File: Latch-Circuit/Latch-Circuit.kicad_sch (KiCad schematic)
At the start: 85 parts, among them J1 BM02B-PASS-1-TF, J10 BM02B-PASS-1-TF, J2 BM03B-PASS-1-TF, J3 BM02B-PASS-1-TF, J4 BM02B-PASS-1-TF, J5 BM02B-PASS-1-TF, J6 BM02B-PASS-1-TF, J7 B2P-VH, J8 BM02B-PASS-1-TF, J9 BM02B-PASS-1-TF, K1 G5Q-1A4_DC12, K2 G5Q-1A4_DC12, K3 G5Q-1A4_DC12, Q1 DMP3098LQ-7, Q10 2N7002K-AU, Q11 2N7002K-AU, Q12 PJA3439-AU_R1_000A1, Q13 PJA3439-AU_R1_000A1, Q2 2N7002K-AU, Q3 PJA3439-AU_R1_000A1, Q4 2N7002K-AU, Q5 PJA3439-AU_R1_000A1, Q6 2N7002K-AU, Q7 2N7002K-AU, Q8 PJA3439-AU_R1_000A1, Q9 PJA3439-AU_R1_000A1

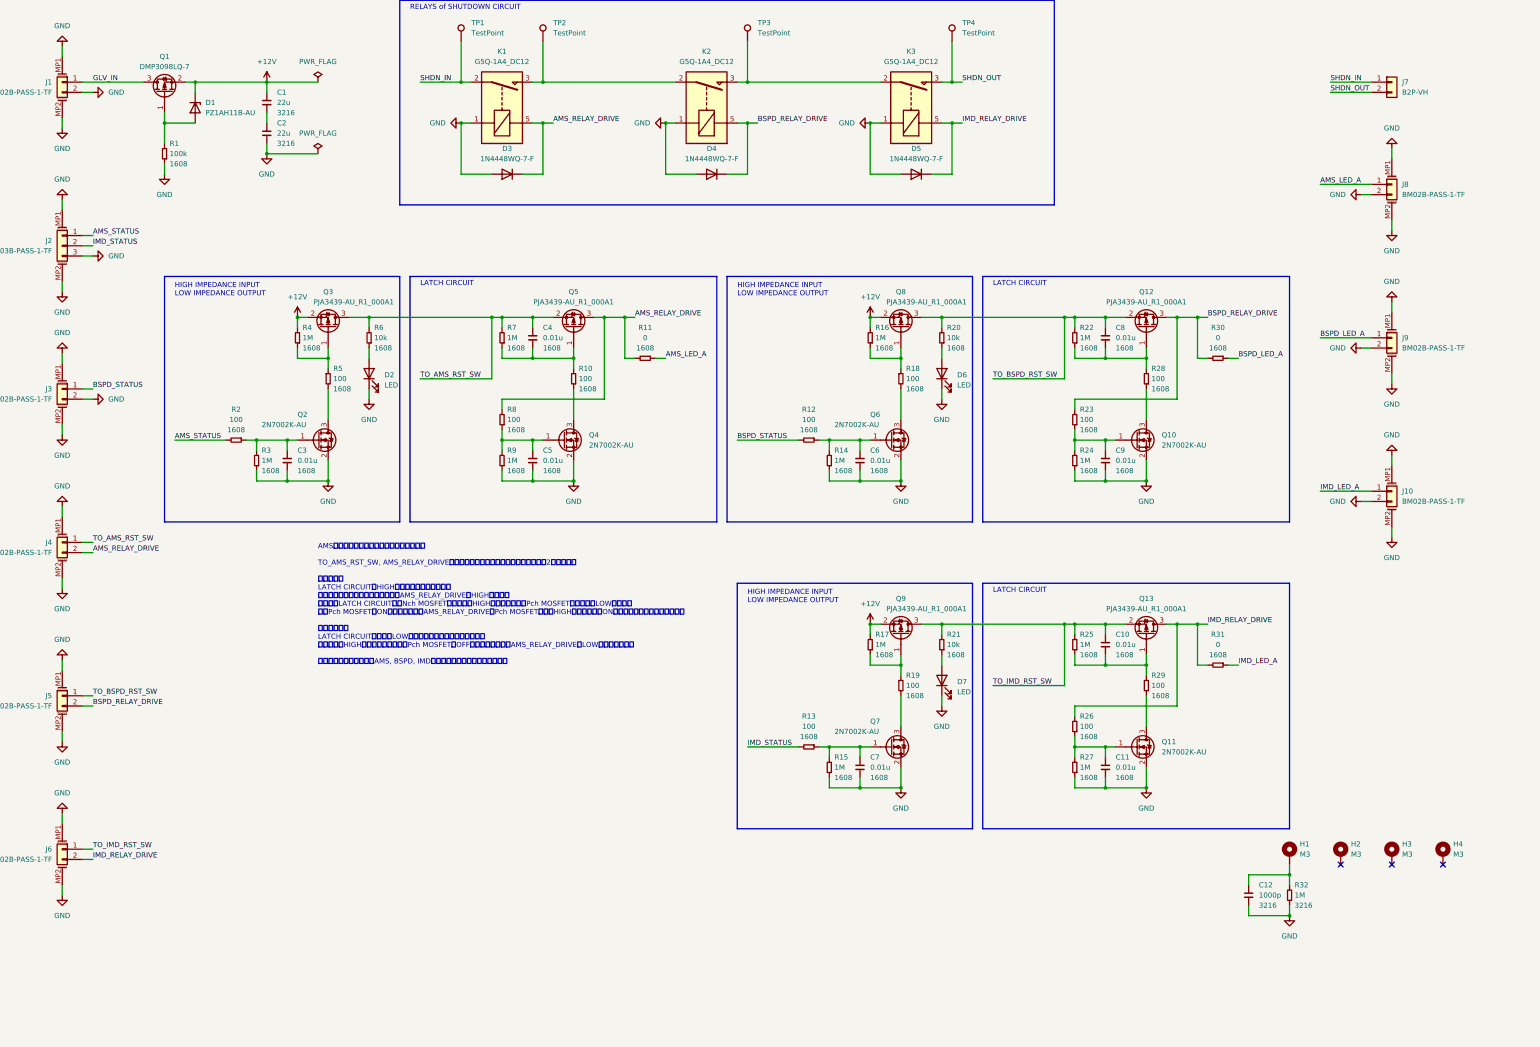
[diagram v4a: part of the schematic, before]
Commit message: modify constant, add circuits Rgs 1M->100k, NOT Circuit for status LED, LED for test
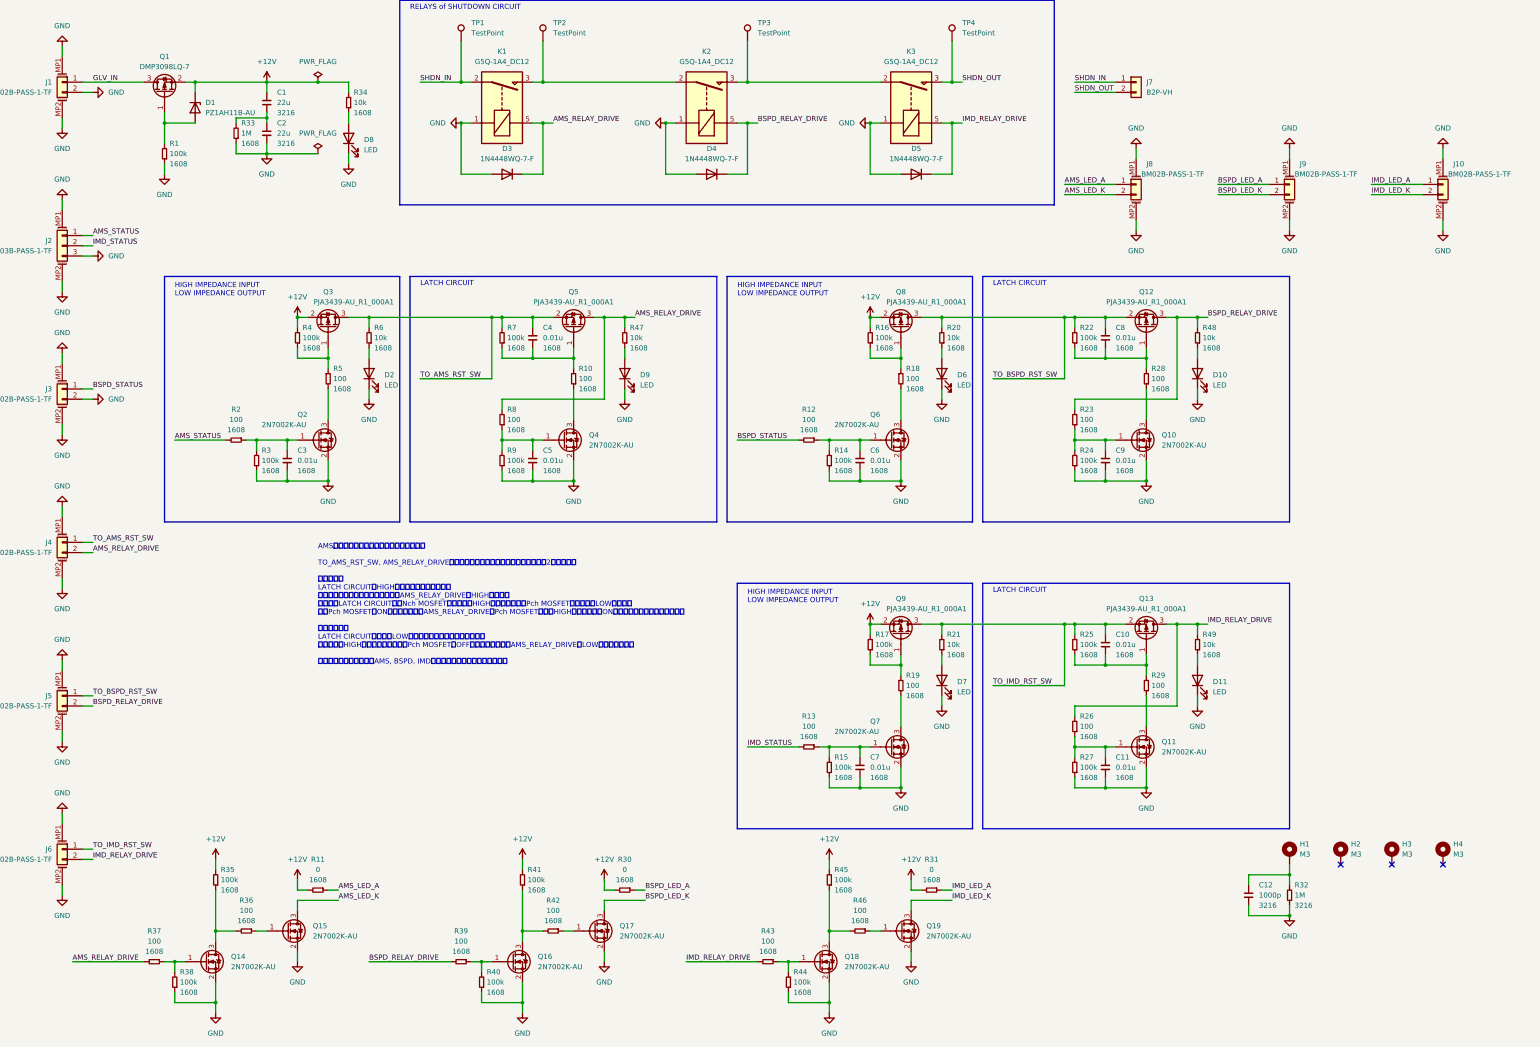
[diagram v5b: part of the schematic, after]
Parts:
- added D10, D11, D8, D9: LED, LED_SMD:LED_0603_1608Metric, symbol Device:LED
- added Q14, Q15, Q16, Q17, Q18, Q19: 2N7002K-AU, ProjectEV:Package_SOT-23_2N7002K-AU, symbol ProjectEV:Transistor_2N7002K-AU
- added R33: 1M, Resistor_SMD:R_0603_1608Metric, symbol ProjectEV:R
- added R34, R47, R48, R49: 10k, Resistor_SMD:R_0603_1608Metric, symbol ProjectEV:R
- added R35, R38, R40, R41, R44, R45: 100k, Resistor_SMD:R_0603_1608Metric, symbol ProjectEV:R
- added R36, R37, R39, R42, R43, R46: 100, Resistor_SMD:R_0603_1608Metric, symbol ProjectEV:R
- R14, R15, R16, R17, R22, R24, R25, R27, R3, R4, R7, R9: value 1M -> 100k
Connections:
- net +12V: now also R11.2, R30.2, R31.2, R34.2, R35.2, R41.2, R45.2
- net AMS_RELAY_DRIVE: now also R37.2, R47.2; no longer R11.2
- net BSPD_RELAY_DRIVE: now also R39.2, R48.2; no longer R30.2
- net GND: now also D10.1 (K), D11.1 (K), D8.1 (K), D9.1 (K), Q14.2 (S), Q15.2 (S), Q16.2 (S), Q17.2 (S), Q18.2 (S), Q19.2 (S), R33.1, R38.1, R40.1, R44.1; no longer J10.2 (Pin_2), J8.2 (Pin_2), J9.2 (Pin_2)
- net IMD_RELAY_DRIVE: now also R43.2, R49.2; no longer R31.2
- net at C1.2, C2.1: now also R33.2
- new net: Q19.1 (G), R46.1
- new net: D8.2 (A), R34.1
- new net: D10.2 (A), R48.1
- new net: Q16.1 (G), R39.1, R40.2
- new net: Q14.1 (G), R37.1, R38.2
- new net: Q14.3 (D), R35.1, R36.2
- new net: Q18.1 (G), R43.1, R44.2
- new net: Q18.3 (D), R45.1, R46.2
- new net: D9.2 (A), R47.1
- new net: Q16.3 (D), R41.1, R42.2
- new net: D11.2 (A), R49.1
- new net: Q17.1 (G), R42.1
- new net: Q15.1 (G), R36.1
- new net AMS_LED_K: J8.2 (Pin_2), Q15.3 (D)
- new net BSPD_LED_K: J9.2 (Pin_2), Q17.3 (D)
- new net IMD_LED_K: J10.2 (Pin_2), Q19.3 (D)
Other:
- moved on the sheet: J10, J7, J8, J9, R11, R30, R31
